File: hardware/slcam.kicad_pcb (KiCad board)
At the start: 2 copper layers, 2 parts, among them U1 STM32F103C8Tx, Y1 Crystal

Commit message: Initial layout
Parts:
- added H1: MountingHole, MountingHole:MountingHole_3mm, F.Cu at (235.4, 53.4)
- added H2: MountingHole, MountingHole:MountingHole_3mm, F.Cu at (235.4, 71.5)
- added J1: 532610671, Connector_Molex:Molex_PicoBlade_53261-0671_1x06-1MP_P1.25mm_Horizontal, F.Cu at (216.9, 70.9)
- added J2: Conn_01x08, Connector_PinHeader_2.54mm:PinHeader_1x08_P2.54mm_Vertical, F.Cu at (205.8, 53.6)
- added J3: Conn_01x04, Connector_PinHeader_2.54mm:PinHeader_1x04_P2.54mm_Vertical, F.Cu at (211.3, 53.1)
- added J4: 532610371, Connector_Molex:Molex_PicoBlade_53261-0371_1x03-1MP_P1.25mm_Horizontal, F.Cu at (234.7, 62.5)
- added U2: W25Q128JVS, Package_SO:SOIC-8_5.23x5.23mm_P1.27mm, F.Cu at (226.2, 57.0)
- added U3: TCAN330G, Package_SO:SOIC-8_3.9x4.9mm_P1.27mm, B.Cu at (226.1, 58.2)
- added U4: TPS2044D, Package_SO:SOIC-16_3.9x9.9mm_P1.27mm, F.Cu at (215.1, 61.0)
- U1: moved to B.Cu
- Y1: value Crystal -> Crystal_GND24; moved to B.Cu
- moved U1 57.4 mm to (217.0, 62.5), turned to 315 degrees
- moved Y1 56.4 mm to (225.8, 68.1)
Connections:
- Y1 pad 3: (no net) -> Net-(Y1-Pad3)
- Y1 pad 4: (no net) -> Net-(Y1-Pad4)
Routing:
- added copper zone on B.Cu, net (none)
- added copper zone on F.Cu, net (none)
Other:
- board outline added: 34.3 x 22.3 mm

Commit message: General fixes #8 #9
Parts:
- added H3: MountingHole, MountingHole:MountingHole_3.2mm_M3_Pad, F.Cu at (235.4, 71.5)
- added H4: MountingHole, MountingHole:MountingHole_3.2mm_M3_Pad, F.Cu at (235.4, 53.4)
- H1, H2: footprint MountingHole:MountingHole_3mm -> MountingHole:MountingHole_3.2mm_M3_Pad
- moved H1 34.4 mm to (200.9, 53.4)
- moved H2 34.4 mm to (200.9, 71.5)
- moved J4 1.78 mm to (236.5, 62.5)
- moved J1 1.52 mm to (216.9, 72.4)
- moved U3 1.36 mm to (227.3, 57.5)
- moved J3 0.80 mm to (211.1, 53.8)
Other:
- board size 34.3 x 22.3 mm -> 42.2 x 25.4 mm

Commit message: Initial layout and schematics fixes
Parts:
- added C1: 1uF, Capacitor_SMD:C_0603_1608Metric_Pad1.05x0.95mm_HandSolder, F.Cu at (223.0, 70.1)
- added C2: 100nF, Capacitor_SMD:C_0603_1608Metric_Pad1.05x0.95mm_HandSolder, F.Cu at (212.0, 56.5)
- added C3: 10nF, Capacitor_SMD:C_0603_1608Metric_Pad1.05x0.95mm_HandSolder, B.Cu at (209.6, 65.4)
- added C4: 10nF, Capacitor_SMD:C_0603_1608Metric_Pad1.05x0.95mm_HandSolder, B.Cu at (213.0, 56.5)
- added C5: 10nF, Capacitor_SMD:C_0603_1608Metric_Pad1.05x0.95mm_HandSolder, B.Cu at (225.3, 61.1)
- added C6: 10nF, Capacitor_SMD:C_0603_1608Metric_Pad1.05x0.95mm_HandSolder, B.Cu at (220.4, 69.3)
- added C7: 20pF, Capacitor_SMD:C_0603_1608Metric_Pad1.05x0.95mm_HandSolder, B.Cu at (226.1, 66.7)
- added C8: 20pF, Capacitor_SMD:C_0603_1608Metric_Pad1.05x0.95mm_HandSolder, B.Cu at (226.1, 70.2)
- added D1: LED, LED_SMD:LED_0603_1608Metric_Pad1.05x0.95mm_HandSolder, F.Cu at (201.1, 61.4)
- added D2: LED, LED_SMD:LED_0603_1608Metric_Pad1.05x0.95mm_HandSolder, F.Cu at (229.4, 73.8)
- added J5: 532610371, Connector_Molex:Molex_PicoBlade_53261-0371_1x03-1MP_P1.25mm_Horizontal, F.Cu at (226.3, 53.1)
- added R1: 10K, Resistor_SMD:R_0603_1608Metric_Pad1.05x0.95mm_HandSolder, F.Cu at (222.7, 66.2)
- added R2: 510, Resistor_SMD:R_0603_1608Metric_Pad1.05x0.95mm_HandSolder, F.Cu at (201.1, 59.8)
- added R3: 510, Resistor_SMD:R_0603_1608Metric_Pad1.05x0.95mm_HandSolder, F.Cu at (226.0, 73.8)
- added R4: 100K, Resistor_SMD:R_0603_1608Metric_Pad1.05x0.95mm_HandSolder, B.Cu at (222.5, 57.2)
- added R5: 100K, Resistor_SMD:R_0603_1608Metric_Pad1.05x0.95mm_HandSolder, B.Cu at (210.9, 67.5)
- added R6: 10K, Resistor_SMD:R_0603_1608Metric_Pad1.05x0.95mm_HandSolder, B.Cu at (200.8, 66.4)
- added R7: 10K, Resistor_SMD:R_0603_1608Metric_Pad1.05x0.95mm_HandSolder, B.Cu at (200.8, 64.9)
- added R8: 120, Resistor_SMD:R_0603_1608Metric_Pad1.05x0.95mm_HandSolder, B.Cu at (238.0, 61.8)
- added R9: 1M, Resistor_SMD:R_0603_1608Metric_Pad1.05x0.95mm_HandSolder, B.Cu at (223.4, 71.1)
- moved U2 10.3 mm to (226.7, 67.3)
- moved Y1 2.46 mm to (223.4, 67.9), turned to 270 degrees
- moved J1 2.09 mm to (214.9, 71.9)
- moved U4 1.14 mm to (215.6, 62.0), turned to 270 degrees
- moved J4 0.51 mm to (236.0, 62.5)
- turned U1 to 135 degrees
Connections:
- J1 pad 1: Net-(J1-Pad1) -> VCC
- J1 pad 2: Net-(J1-Pad2) -> GND
- J1 pad 3: Net-(J1-Pad3) -> /SPI_MOSI
- J1 pad 4: Net-(J1-Pad4) -> /SPI_MISO
- J1 pad 5: Net-(J1-Pad5) -> /SPI_SCK
- J1 pad 6: Net-(J1-Pad6) -> /SPI_NSS
- J2 pad 1: Net-(J2-Pad1) -> /SPI_NSS_IMG
- J2 pad 2: Net-(J2-Pad2) -> /SPI_MOSI
- J2 pad 3: Net-(J2-Pad3) -> /SPI_MISO
- J2 pad 4: Net-(J2-Pad4) -> /SPI_SCK
- J2 pad 5: Net-(J2-Pad5) -> GND
- J2 pad 6: Net-(J2-Pad6) -> /3V3_IMG_SENSOR
- J2 pad 7: Net-(J2-Pad7) -> /I2C_SDA
- J2 pad 8: Net-(J2-Pad8) -> /I2C_SCL
- J3 pad 1: Net-(J3-Pad1) -> GND
- J3 pad 2: Net-(J3-Pad2) -> VCC
- J3 pad 3: Net-(J3-Pad3) -> /SWCLK
- J3 pad 4: Net-(J3-Pad4) -> /SWDIO
- J4 pad 1: Net-(J4-Pad1) -> GND
- J4 pad 2: Net-(J4-Pad2) -> /CAN_P
- J4 pad 3: Net-(J4-Pad3) -> /CAN_N
- U1 pad 12: Net-(U1-Pad12) -> /SPI_NSS_IMG
- U1 pad 13: Net-(U1-Pad13) -> /SPI_NSS_FLASH
- U1 pad 14: Net-(U1-Pad14) -> /SPI_NSS
- U1 pad 15: Net-(U1-Pad15) -> /SPI_SCK
- U1 pad 16: Net-(U1-Pad16) -> /SPI_MISO
- U1 pad 17: Net-(U1-Pad17) -> /SPI_MOSI
- U1 pad 18: Net-(U1-Pad18) -> /EN_SWITCH
- U1 pad 2: Net-(U1-Pad2) -> /HEARTBEAT
- U1 pad 20: Net-(U1-Pad20) -> /BOOT1
- U1 pad 24: Net-(U1-Pad24) -> VCC
- U1 pad 30: Net-(U1-Pad30) -> /UART_TX
- U1 pad 31: Net-(U1-Pad31) -> /UART_RX
- U1 pad 32: Net-(U1-Pad32) -> /CAN_RX
- U1 pad 33: Net-(U1-Pad33) -> /CAN_TX
- U1 pad 34: Net-(U1-Pad34) -> /SWDIO
- U1 pad 36: Net-(U1-Pad36) -> VCC
- U1 pad 37: Net-(U1-Pad37) -> /SWCLK
- U1 pad 42: Net-(U1-Pad42) -> /I2C_SCL
- U1 pad 43: Net-(U1-Pad43) -> /I2C_SDA
- U1 pad 44: Net-(U1-Pad44) -> /BOOT0
- U1 pad 48: Net-(U1-Pad48) -> VCC
- U1 pad 5: Net-(U1-Pad5) -> /OSC_IN
- U1 pad 6: Net-(U1-Pad6) -> /OSC_OUT
- U1 pad 7: Net-(U1-Pad7) -> /RESET
- U1 pad 9: Net-(U1-Pad9) -> VCC
- U2 pad 1: Net-(U2-Pad1) -> /SPI_NSS_FLASH
- U2 pad 2: Net-(U2-Pad2) -> /SPI_MOSI
- U2 pad 4: Net-(U2-Pad4) -> GND
- U2 pad 5: Net-(U2-Pad5) -> /SPI_MISO
- U2 pad 6: Net-(U2-Pad6) -> /SPI_SCK
- U2 pad 8: Net-(U2-Pad8) -> VCC
- U3 pad 1: Net-(U3-Pad1) -> /CAN_TX
- U3 pad 2: Net-(U3-Pad2) -> GND
- U3 pad 3: Net-(U3-Pad3) -> VCC
- U3 pad 4: Net-(U3-Pad4) -> /CAN_RX
- U3 pad 6: Net-(U3-Pad6) -> /CAN_N
- U3 pad 7: Net-(U3-Pad7) -> /CAN_P
- U4 pad 1: Net-(U4-Pad1) -> GND
- U4 pad 15: Net-(U4-Pad15) -> /3V3_IMG_SENSOR
- U4 pad 2: Net-(U4-Pad2) -> VCC
- U4 pad 3: Net-(U4-Pad3) -> /EN_SWITCH
- U4 pad 4: Net-(U4-Pad4) -> VCC
- Y1 pad 1: Net-(Y1-Pad1) -> /OSC_IN
- Y1 pad 2: Net-(Y1-Pad2) -> GND
- Y1 pad 3: Net-(Y1-Pad3) -> /OSC_OUT
- Y1 pad 4: Net-(Y1-Pad4) -> GND
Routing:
- net GND: track 0.00 -> 28.7 mm
- net VCC: track 0.00 -> 26.8 mm, vias 0 -> 1
- net /CAN_P: track 0.00 -> 13.9 mm, vias 0 -> 2
- net /CAN_N: track 0.00 -> 12.3 mm, vias 0 -> 2
- net /OSC_OUT: track 0.00 -> 12.3 mm
- net /I2C_SCL: track 0.00 -> 7.51 mm
- net /SWDIO: track 0.00 -> 7.27 mm
- net /OSC_IN: track 0.00 -> 7.25 mm
- net /RESET: track 0.00 -> 5.98 mm, vias 0 -> 1
- net /I2C_SDA: track 0.00 -> 5.73 mm
- net Net-(C7-Pad2): track 0.00 -> 4.75 mm
- net /SWCLK: track 0.00 -> 4.53 mm, vias 0 -> 1
- net /BOOT0: track 0.00 -> 2.94 mm
- net /BOOT1: track 0.00 -> 2.78 mm
- net Net-(D1-Pad1): track 0.00 -> 2.40 mm

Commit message: Hardware: Developing Layout #23
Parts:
- moved C2 0.10 mm to (212.0, 56.4)
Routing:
- net VCC: track 26.8 -> 97.9 mm, vias 1 -> 6
- net /SPI_MOSI: track 0.00 -> 68.1 mm, vias 0 -> 1
- net /SPI_MISO: track 0.00 -> 60.2 mm, vias 0 -> 2
- net /SPI_SCK: track 0.00 -> 59.1 mm, vias 0 -> 3
- net /I2C_SCL: track 7.51 -> 47.8 mm, vias 0 -> 1
- net /UART_RX: track 0.00 -> 35.2 mm, vias 0 -> 1
- net /UART_TX: track 0.00 -> 34.6 mm, vias 0 -> 1
- net /SPI_NSS_IMG: track 0.00 -> 29.3 mm
- net GND: track 28.7 -> 3.32 mm
- net /SPI_NSS_FLASH: track 0.00 -> 23.8 mm, vias 0 -> 1
- net /I2C_SDA: track 5.73 -> 28.4 mm, vias 0 -> 1
- net /CAN_RX: track 0.00 -> 22.5 mm
- net /CAN_TX: track 0.00 -> 21.5 mm
- net /EN_SWITCH: track 0.00 -> 21.1 mm, vias 0 -> 1
- net /3V3_IMG_SENSOR: track 0.00 -> 19.7 mm, vias 0 -> 2
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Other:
- net class Default removed

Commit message: Hardware: Developing Layout #23
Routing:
- net /SPI_NSS: track 0.00 -> 16.1 mm, vias 0 -> 2
- net /SPI_SCK: track 59.1 -> 66.7 mm
- net /OSC_IN: track 7.25 -> 11.5 mm
- net /SPI_MISO: track 60.2 -> 62.2 mm
- net /BOOT1: track 2.78 -> 2.16 mm
- net /SPI_MOSI: track 68.1 -> 67.6 mm
- net VCC: track 97.9 -> 97.8 mm, vias 6 -> 7
- net GND: vias 0 -> 1
- added copper zone on B.Cu, net GND
- added copper zone on F.Cu, net GND
- added copper zone on In1.Cu, net VCC
- added copper zone on In2.Cu, net VCC
- removed copper zone on B.Cu, net (none)
- removed copper zone on F.Cu, net (none)
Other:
- copper layers 2 -> 4

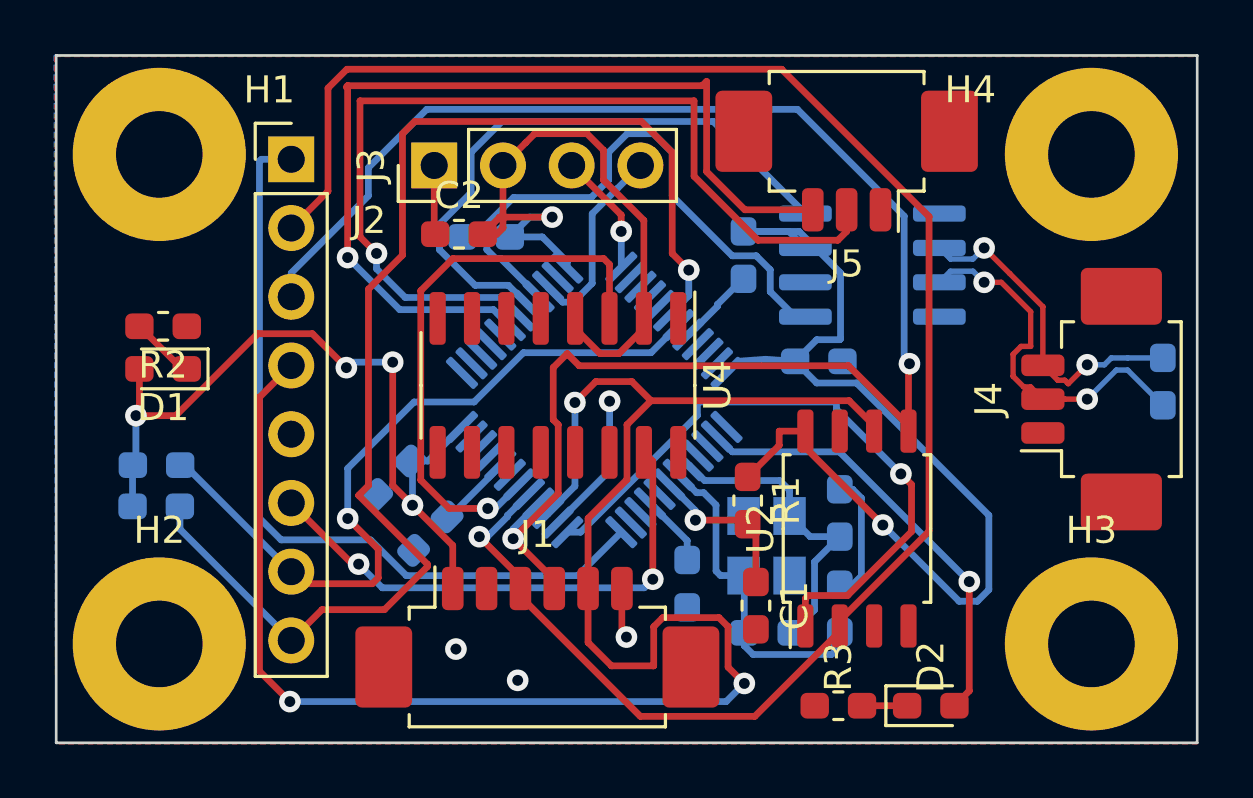
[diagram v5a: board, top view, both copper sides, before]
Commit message: Hardware: finishing layout, just missing footprints #23
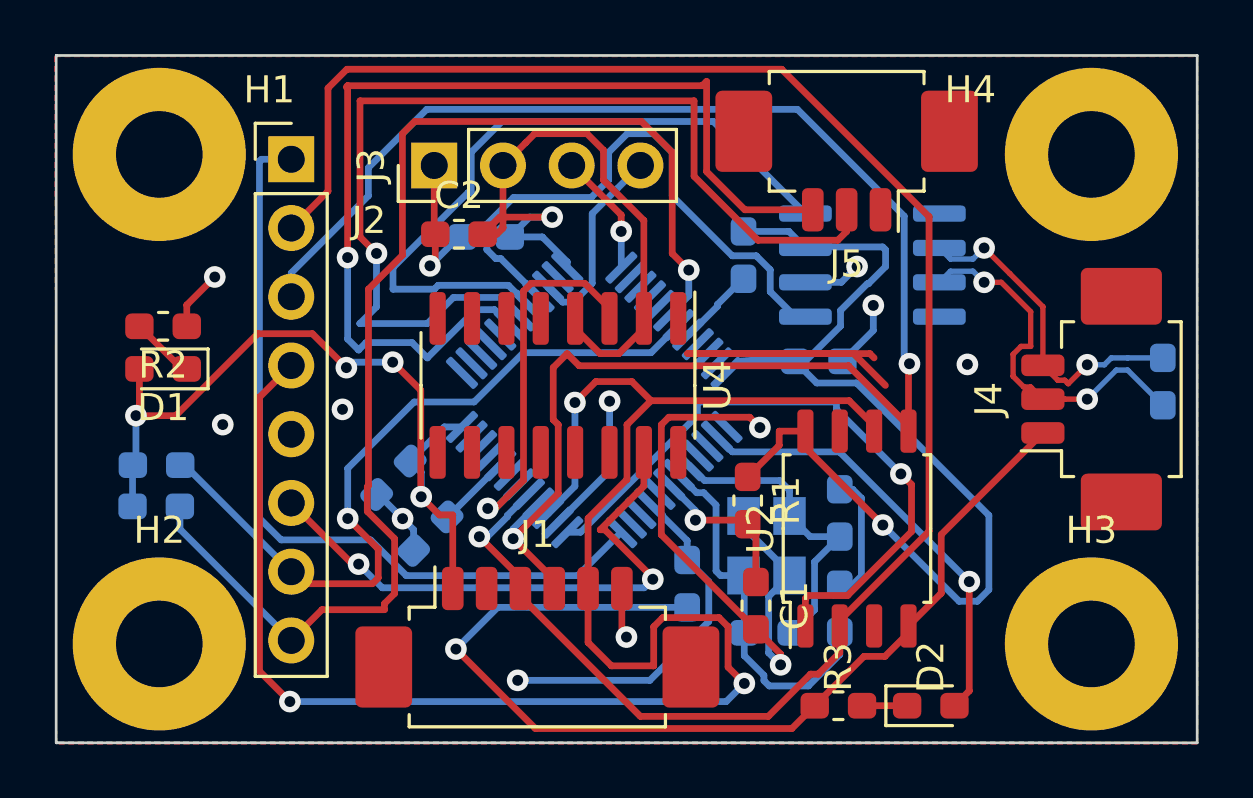
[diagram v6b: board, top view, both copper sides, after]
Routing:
- net GND: track 3.32 -> 146.4 mm, vias 1 -> 11
- net (no net): track 0.00 -> 14.8 mm
- net VCC: track 97.8 -> 109.4 mm
- net /EN_SWITCH: track 21.0 -> 14.3 mm
- net /UART_TX: track 34.6 -> 38.1 mm
- net /CAN_RX: track 22.5 -> 26.0 mm
- net /UART_RX: track 35.2 -> 38.0 mm
- net /OSC_OUT: track 12.3 -> 13.8 mm
- net /3V3_IMG_SENSOR: track 19.7 -> 21.1 mm
- net /I2C_SCL: track 47.8 -> 46.5 mm
- net /BOOT1: track 2.16 -> 2.79 mm
